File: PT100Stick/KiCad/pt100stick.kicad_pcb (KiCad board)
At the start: 2 copper layers, 15.2 x 20.3 mm, 13 parts, among them U1 MAX31865ATP_, U2 MCP1799T-3302H

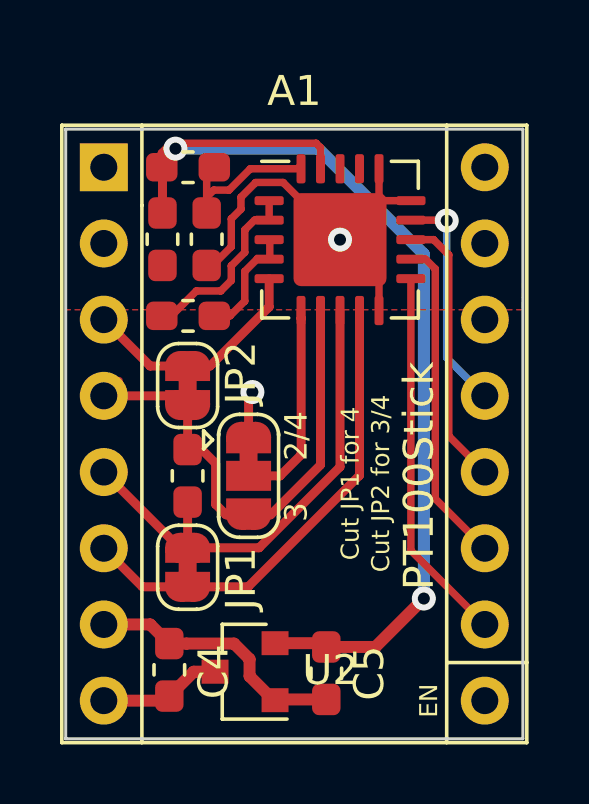
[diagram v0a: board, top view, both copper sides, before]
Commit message: PT100 update (#84)
* Add 2.2uF cap

* add gerberzip

* Fix silkscreen overlaps.
Update some docs
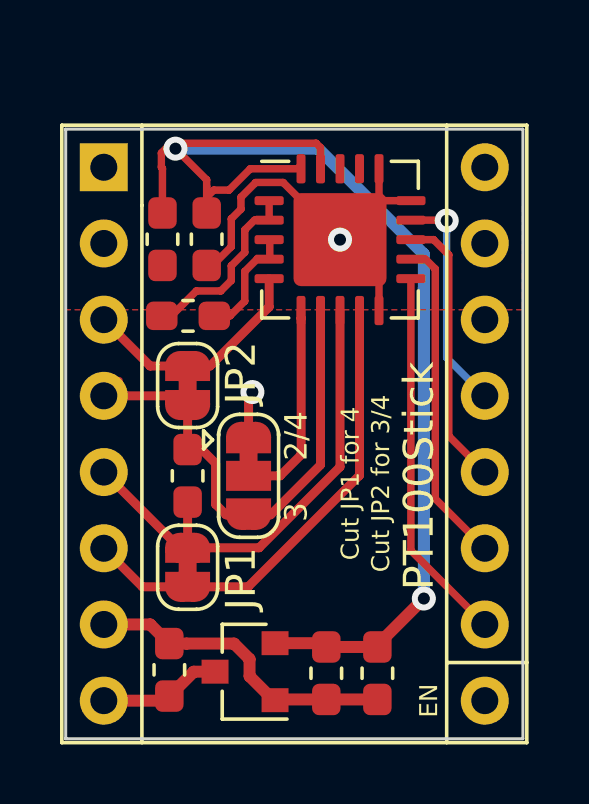
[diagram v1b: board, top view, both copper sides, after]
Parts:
- removed FB1: Ferrite_Bead_Small, PT100Stick:L_0603_1608Metric_Pad1.05x0.95mm_HandSolder
- added C6: 2.2uF, PT100Stick:C_0603_1608Metric_Pad1.05x0.95mm_HandSolder, F.Cu at (151.4, 88.0)
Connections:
- C3 pad 1: VDDA -> +3V3
- U1 pad 20: VDDA -> +3V3
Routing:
- net +3V3: track 36.0 -> 42.5 mm
- net VDDA: track 5.80 -> 0.00 mm
- net GND: track 24.5 -> 26.2 mm
